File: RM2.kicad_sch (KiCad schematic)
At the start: 7 parts, among them U2 RM2

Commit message: Complete schematic for first prototype
- Footprints: passives 0402/0603 (larger only for 24 V / DC bias),
  U1 and L1 footprints taken from RP2350A Minimal R4 reference (MIT)
- New sheet vystupy: heater (Q1 SiS434DN) with thermal fuse terminal J13,
  fan (GPIO13) and exhaust fan (GPIO12) with AO3422, input protection
  (fuse, AOD4185 reverse polarity, SMBJ24CA TVS, bulk cap), status LED on
  RM2 GPIO0, button GPIO15, NTC on ADC0 (22k pull-up), I2C1 pull-ups,
  second SHT40 on I2C0 (GPIO8/9)
- New sheet rozsireni: spare GPIO header J12, test points TP1-TP5,
  mounting holes H1-H4
- Selected parts with Manufacturer/MPN fields; L2 4.7 uH Wurth 74438356047
- Fix D2 pin mapping (Device:D_Schottky), remove duplicate pull-down R12,
  C16 changed to 100 nF for third DVDD pin, Y1 value set
- Project footprint library susicka.pretty (PowerPAK 1212-8 with G/S/D pads)

Co-Authored-By: Claude Opus 5.5 <noreply@anthropic.com>
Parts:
- removed R12: 10k, Resistor_SMD:R_0603_1608Metric, symbol Device:R
- C18: footprint Capacitor_SMD:C_0603_1608Metric -> Capacitor_SMD:C_0402_1005Metric
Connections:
- net WL_GPIO0: now reaches U2.8 (GPIO0)
- no-connect marks 3 -> 2
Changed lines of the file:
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@@
-	)
-	(junction
-		(at 134.62 120.65)
-		(diameter 0)
-		(color 0 0 0 0)
 	)
 	(junction
@@
 	)
 	(no_connect
-		(at 121.92 102.87)
-	)
-	(no_connect
 		(at 148.59 83.82)
 	)
@@
 	(wire
 		(pts
-			(xy 134.62 120.65) (xy 139.7 120.65)
-		)
-		(stroke
-			(width 0)
-			(type default)
-		)
-	)
-	(wire
-		(pts
 			(xy 132.08 102.87) (xy 132.08 116.84)
 		)
@@
 		(pts
 			(xy 137.16 105.41) (xy 137.16 107.95)
-		)
-		(stroke
-			(width 0)
-			(type default)
-		)
-	)
-	(wire
-		(pts
-			(xy 147.32 120.65) (xy 152.4 120.65)
 		)
 		(stroke
@@
 	(symbol
 		(lib_id "power:GND")
-		(at 152.4 120.65 90)
-		(unit 1)
-		(exclude_from_sim no)
-		(in_bom yes)
-		(on_board yes)
-		(dnp no)
-		(fields_autoplaced yes)
-		(property "Reference" "#PWR032"
-			(at 158.75 120.65 0)
-			(effects
-				(font
-					(size 1.27 1.27)
-				)
-				(hide yes)
-			)
-		)
-		(property "Value" "GND"
-			(at 156.21 120.6499 90)
-			(effects
-				(font
-					(size 1.27 1.27)
-				)
-				(justify right)
-			)
-		)
-		(property "Footprint" ""
-			(at 152.4 120.65 0)
-			(effects
-				(font
-					(size 1.27 1.27)
-				)
-				(hide yes)
-			)
-		)
-		(property "Datasheet" ""
-			(at 152.4 120.65 0)
-			(effects
-				(font
-					(size 1.27 1.27)
-				)
-				(hide yes)
-			)
-		)
-		(property "Description" "Power symbol creates a global label with name \"GND\" , ground"
-			(at 152.4 120.65 0)
-			(effects
-				(font
-					(size 1.27 1.27)
-				)
-				(hide yes)
-			)
-		)
-		(pin "1"
-		)
-		(instances
-			(project "susicka_filamentu"
-				(path "/202a5452-a4a8-46b1-91e1-aa7f241e9adc/2d41c25d-4508-4be3-abef-357e16c44385"
-					(reference "#PWR032")
-					(unit 1)
-				)
-			)
-		)
-	)
-	(symbol
-		(lib_id "power:GND")
 		(at 106.68 76.2 270)
 		(unit 1)
@@
 	)
 	(symbol
-		(lib_id "Device:R")
-		(at 143.51 120.65 90)
-		(unit 1)
-		(exclude_from_sim no)
-		(in_bom yes)
-		(on_board yes)
-		(dnp no)
-		(property "Reference" "R12"
-			(at 141.986 123.952 90)
-			(effects
-				(font
-					(size 1.27 1.27)
-				)
-			)
-		)
-		(property "Value" "10k"
-			(at 141.986 125.73 90)
-			(effects
-				(font
-					(size 1.27 1.27)
-				)
-			)
-		)
-		(property "Footprint" "Resistor_SMD:R_0603_1608Metric"
-			(at 143.51 122.428 90)
-			(effects
-				(font
-					(size 1.27 1.27)
-				)
-				(hide yes)
-			)
-		)
-		(property "Datasheet" "~"
-			(at 143.51 120.65 0)
-			(effects
-				(font
-					(size 1.27 1.27)
-				)
-				(hide yes)
-			)
-		)
-		(property "Description" "Resistor"
-			(at 143.51 120.65 0)
-			(effects
-				(font
-					(size 1.27 1.27)
-				)
-				(hide yes)
-			)
-		)
-		(pin "1"
-		)
-		(pin "2"
-		)
-		(instances
-			(project ""
-				(path "/202a5452-a4a8-46b1-91e1-aa7f241e9adc/2d41c25d-4508-4be3-abef-357e16c44385"
-					(reference "R12")
-					(unit 1)
-				)
-			)
-		)
-	)
-	(symbol
 		(lib_id "power:GND")
 		(at 153.67 91.44 90)
@@
 			)
 		)
-		(property "Footprint" "Capacitor_SMD:C_0603_1608Metric"
+		(property "Footprint" "Capacitor_SMD:C_0402_1005Metric"
 			(at 144.78 104.4448 0)
 			(effects
@@
 			)
 		)
+	)
+	(wire
+		(pts
+			(xy 121.92 102.87) (xy 121.92 105.41)
+		)
+		(stroke
+			(width 0)
+			(type default)
+		)
+	)
+	(global_label "WL_GPIO0"
+		(shape output)
+		(at 121.92 105.41 270)
+		(fields_autoplaced yes)
+		(effects
+			(font
+				(size 1.27 1.27)
+			)
+			(justify right)
+		)
+		(property "Intersheetrefs" "${INTERSHEET_REFS}"
+			(at 121.92 105.41 0)
+			(effects
+				(font
+					(size 1.27 1.27)
+				)
+				(justify right)
+				(hide yes)
+			)
+		)

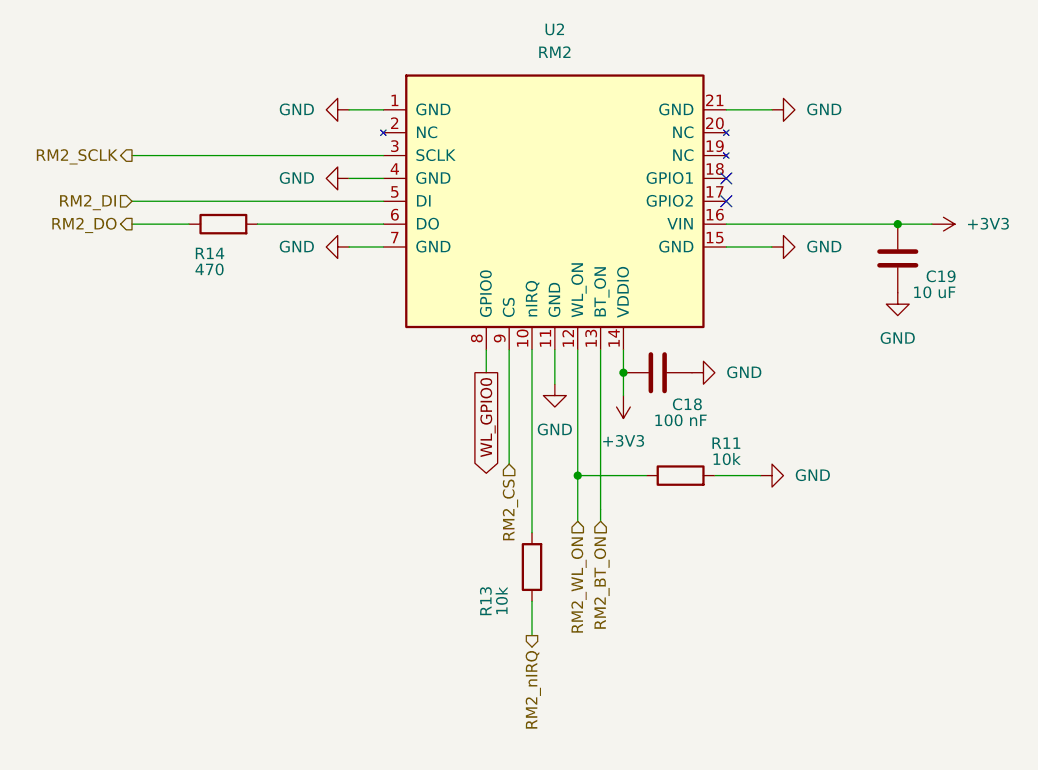
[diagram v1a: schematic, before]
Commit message: Layout progress, VREG per reference, SI simulation, project notes
- Board: 70x100 mm outline, mounting holes, crystal, RP2350 decoupling,
  VREG copied from RP2350A Minimal R4 (zones, priorities, PGND track),
  RM2 placement and gSPI routing (CLK 16.5 mm, DATA 14.4 mm),
  RF keep-out rule area on all copper layers, test points TP12-TP15
- C4/C5/C6/R7 in 0402; C5/C6 use susicka:C_0402_1005Metric_RPi
  (0.56 mm pad gap so VREG_LX passes under the caps)
- simulace/wl_clk: KiCad ngspice model of WL_CLK (TLINE Z0 ~94 ohm,
  td ~96 ps) for transient and AC (Bode) analysis
- CLAUDE.md and Claude subagents (.claude/agents) moved into the PCB
  branch so the project context is available on other machines
- Ignore KiCad #auto_saved_files#

Co-Authored-By: Claude Opus 5.5 <noreply@anthropic.com>
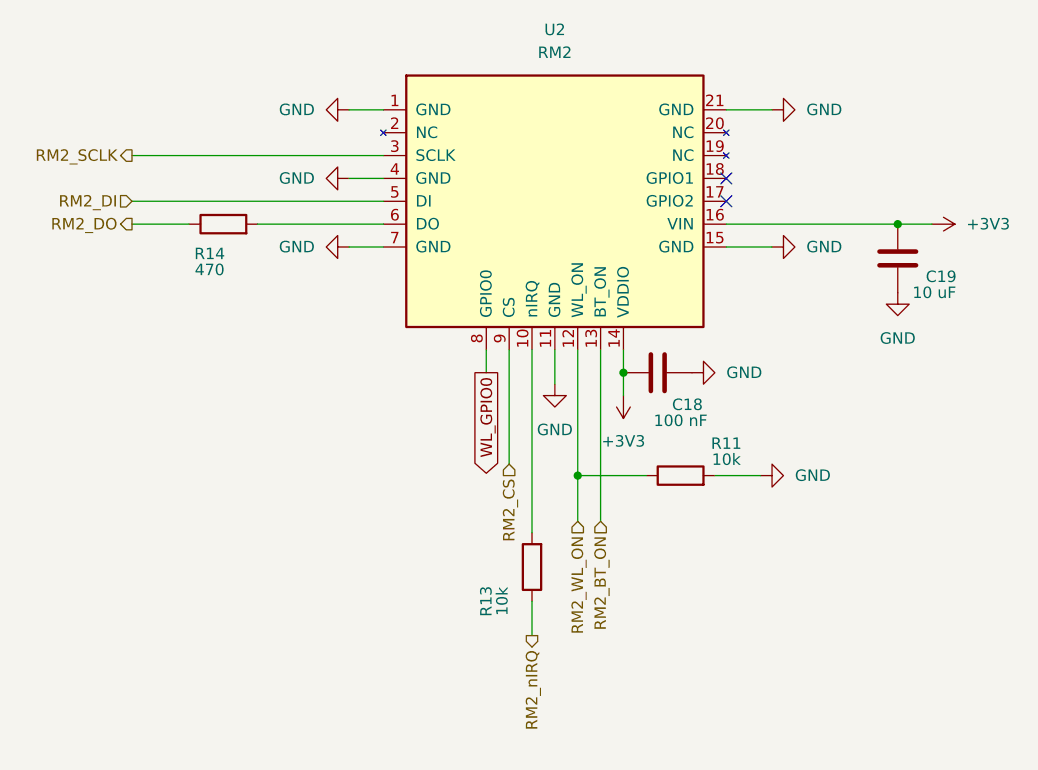
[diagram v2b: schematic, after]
